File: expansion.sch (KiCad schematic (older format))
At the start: 3 parts, among them J7 DF40HC(3.5)-60DS, J9 DF40HC(3.5)-60DS, U1 IMX8MM

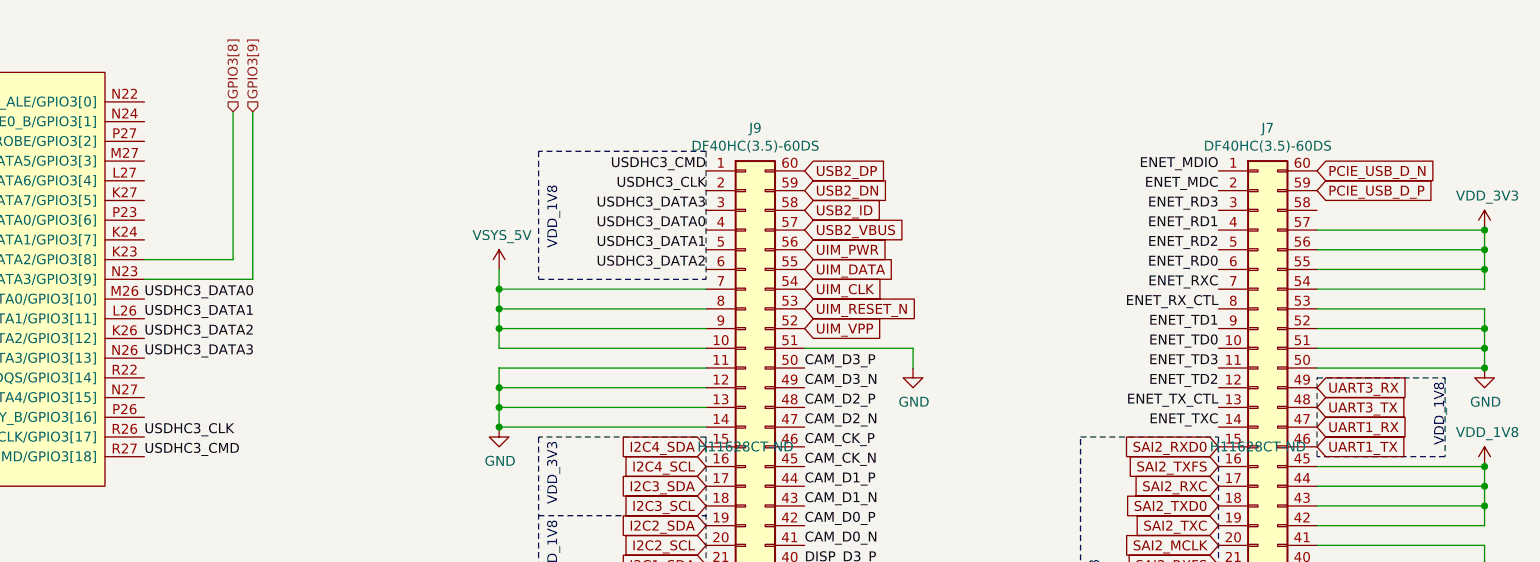
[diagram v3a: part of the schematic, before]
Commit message: Cleanup remaining DRC problems from schematic
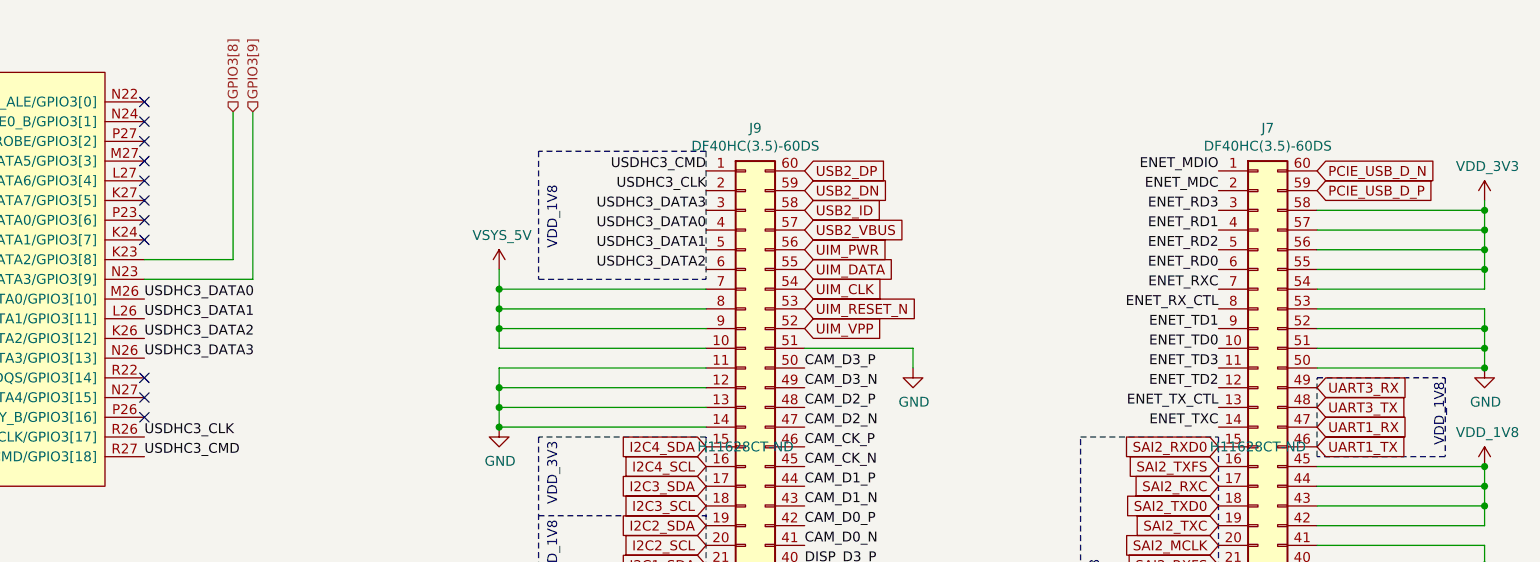
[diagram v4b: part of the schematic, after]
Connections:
- net VDD_3V3: now also J7.58 (Pin_58)
- no-connect marks 0 -> 11
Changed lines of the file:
@@
 L mxenc:VDD_3V3 #PWR0245
 U 1 1 5F185D48
-P 9950 1700
-F 0 "#PWR0245" H 9950 1550 50  0001 C CNN
-F 1 "VDD_3V3" H 9965 1873 50  0000 C CNN
-F 2 "" H 9950 1700 50  0001 C CNN
-F 3 "" H 9950 1700 50  0001 C CNN
-	1    9950 1700
+P 9950 1550
+F 0 "#PWR0245" H 9950 1400 50  0001 C CNN
+F 1 "VDD_3V3" H 9965 1723 50  0000 C CNN
+F 2 "" H 9950 1550 50  0001 C CNN
+F 3 "" H 9950 1550 50  0001 C CNN
+	1    9950 1550
 	1    0    0    -1
 $EndComp
@@
 Wire Wire Line
 	8850 4500 8850 4550
+NoConn ~ 3150 1050
+NoConn ~ 3150 1150
+NoConn ~ 3150 1250
+NoConn ~ 3150 1350
+NoConn ~ 3150 1450
+NoConn ~ 3150 1550
+NoConn ~ 3150 1650
+NoConn ~ 3150 1750
+NoConn ~ 3150 2450
+NoConn ~ 3150 2550
+NoConn ~ 3150 2650
+Wire Wire Line
+	9950 1550 9950 1600
+Wire Wire Line
+	9950 1600 9100 1600
+Connection ~ 9950 1600
+Wire Wire Line
+	9950 1600 9950 1700
 $EndSCHEMATC

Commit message: Re-annotate schematics, add dnp field, and silkscreen cleanup
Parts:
- U1: Mfgr (none) -> NXP; Part (none) -> MIMX8MM6CVTKZAA; Vendorpart (none) -> 568-15276-ND
- renumbered J9 to J11, J7 to J12
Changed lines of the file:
@@
 P 6200 2800
 AR Path="/5E367446" Ref="J?"  Part="1"
-AR Path="/5E34BAA5/5E367446" Ref="J9"  Part="1"
-F 0 "J9" H 6250 4417 50  0000 C CNN
+AR Path="/5E34BAA5/5E367446" Ref="J11"  Part="1"
+F 0 "J11" H 6250 4417 50  0000 C CNN
 F 1 "DF40HC(3.5)-60DS" H 6250 4326 50  0000 C CNN
 F 2 "mxenc:DF40C-60DP" H 6200 2800 50  0001 C CNN
@@
 P 8800 2800
 AR Path="/5E36744C" Ref="J?"  Part="1"
-AR Path="/5E34BAA5/5E36744C" Ref="J7"  Part="1"
-F 0 "J7" H 8850 4417 50  0000 C CNN
+AR Path="/5E34BAA5/5E36744C" Ref="J12"  Part="1"
+F 0 "J12" H 8850 4417 50  0000 C CNN
 F 1 "DF40HC(3.5)-60DS" H 8850 4326 50  0000 C CNN
 F 2 "mxenc:DF40C-60DP" H 8800 2800 50  0001 C CNN
@@
 USB2_ID
 $Comp
-L power:GND #PWR0151
+L power:GND #PWR0192
 U 1 1 5E62C901
 P 6250 4550
-F 0 "#PWR0151" H 6250 4300 50  0001 C CNN
+F 0 "#PWR0192" H 6250 4300 50  0001 C CNN
 F 1 "GND" H 6255 4377 50  0000 C CNN
 F 2 "" H 6250 4550 50  0001 C CNN
@@
 $EndComp
 $Comp
-L power:GND #PWR0152
+L power:GND #PWR0193
 U 1 1 5E62D325
 P 8850 4550
-F 0 "#PWR0152" H 8850 4300 50  0001 C CNN
+F 0 "#PWR0193" H 8850 4300 50  0001 C CNN
 F 1 "GND" H 8855 4377 50  0000 C CNN
 F 2 "" H 8850 4550 50  0001 C CNN
@@
 F 2 "mxenc:BGA-729_27x27_14.0x14.0mm" H 2300 6350 50  0001 C CNN
 F 3 "" H 1300 6350 50  0001 C CNN
+F 4 "NXP" H 2050 3600 50  0001 C CNN "Mfgr"
+F 5 "MIMX8MM6CVTKZAA" H 2050 3600 50  0001 C CNN "Part"
+F 6 "568-15276-ND" H 2050 3600 50  0001 C CNN "Vendorpart"
 	8    2050 3600
 	1    0    0    -1
@@
 F 2 "mxenc:BGA-729_27x27_14.0x14.0mm" H 4550 7400 50  0001 C CNN
 F 3 "" H 3500 7400 50  0001 C CNN
+F 4 "NXP" H 4300 4650 50  0001 C CNN "Mfgr"
+F 5 "MIMX8MM6CVTKZAA" H 4300 4650 50  0001 C CNN "Part"
+F 6 "568-15276-ND" H 4300 4650 50  0001 C CNN "Vendorpart"
 	10   4300 4650
 	1    0    0    1
@@
 UIM_VPP
 $Comp
-L power:GND #PWR0219
+L power:GND #PWR0187
 U 1 1 5F4229EE
 P 7050 2400
-F 0 "#PWR0219" H 7050 2150 50  0001 C CNN
+F 0 "#PWR0187" H 7050 2150 50  0001 C CNN
 F 1 "GND" H 7055 2227 50  0000 C CNN
 F 2 "" H 7050 2400 50  0001 C CNN
@@
 	4950 2100 4950 2000
 $Comp
-L power:GND #PWR0221
+L power:GND #PWR0189
 U 1 1 5F42D118
 P 4950 2700
-F 0 "#PWR0221" H 4950 2450 50  0001 C CNN
+F 0 "#PWR0189" H 4950 2450 50  0001 C CNN
 F 1 "GND" H 4955 2527 50  0000 C CNN
 F 2 "" H 4950 2700 50  0001 C CNN
@@
 Connection ~ 4950 2600
 $Comp
-L mxenc:VDD_1V8 #PWR0223
+L mxenc:VDD_1V8 #PWR0190
 U 1 1 5F46F757
 P 9950 2900
-F 0 "#PWR0223" H 9950 2750 50  0001 C CNN
+F 0 "#PWR0190" H 9950 2750 50  0001 C CNN
 F 1 "VDD_1V8" H 9965 3073 50  0000 C CNN
 F 2 "" H 9950 2900 50  0001 C CNN
@@
 GPIO1[15]
 $Comp
-L power:GND #PWR0222
+L power:GND #PWR0191
 U 1 1 5EFF4815
 P 9950 3600
-F 0 "#PWR0222" H 9950 3350 50  0001 C CNN
+F 0 "#PWR0191" H 9950 3350 50  0001 C CNN
 F 1 "GND" H 9955 3427 50  0000 C CNN
 F 2 "" H 9950 3600 50  0001 C CNN
@@
 	9950 3400 9950 3500
 $Comp
-L mxenc:VDD_3V3 #PWR0245
+L mxenc:VDD_3V3 #PWR0185
 U 1 1 5F185D48
 P 9950 1550
-F 0 "#PWR0245" H 9950 1400 50  0001 C CNN
+F 0 "#PWR0185" H 9950 1400 50  0001 C CNN
 F 1 "VDD_3V3" H 9965 1723 50  0000 C CNN
 F 2 "" H 9950 1550 50  0001 C CNN
@@
 Connection ~ 9950 1800
 $Comp
-L power:GND #PWR0253
+L power:GND #PWR0188
 U 1 1 5F18CEE2
 P 9950 2400
-F 0 "#PWR0253" H 9950 2150 50  0001 C CNN
+F 0 "#PWR0188" H 9950 2150 50  0001 C CNN
 F 1 "GND" H 9955 2227 50  0000 C CNN
 F 2 "" H 9950 2400 50  0001 C CNN
@@
 Connection ~ 9950 1900
 $Comp
-L mxenc:VSYS_5V #PWR0220
+L mxenc:VSYS_5V #PWR0186
 U 1 1 5E69C086
 P 4950 1900
-F 0 "#PWR0220" H 4950 1750 50  0001 C CNN
+F 0 "#PWR0186" H 4950 1750 50  0001 C CNN
 F 1 "VSYS_5V" H 4965 2073 50  0000 C CNN
 F 2 "" H 4950 1900 50  0001 C CNN
